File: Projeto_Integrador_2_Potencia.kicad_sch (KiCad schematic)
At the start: 18 parts, among them J10 Borne_CMD_Interface, J2 Vi 24V, J3 Vo 48V, J4 INA219_01x02_Socket_3.5mm, J5 INA219_01x06_Socket_2.55mm, J7 Display_01x04_Socket, J9 JST_01x02_Pin, Q1 IRF740

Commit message: Adição de footprint e símbolo do ESP32
Atualização das trilhas da PCB
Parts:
- removed ESP32_Socket_L, ESP32_Socket_R: ~, Connector_PinSocket_2.54mm:PinSocket_1x15_P2.54mm_Vertical, symbol Connector:Conn_01x15_Socket
- added U1: ESP32-DEVKIT-V1, footprints_and_symbols:MODULE_ESP32_DEVKIT_V1, symbol ESP32-DEVKIT-V1:ESP32-DEVKIT-V1
- J9: value JST_01x02_Pin -> PWM_Connector
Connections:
- net 12V: now also U1.30 (VIN)
- net 3V3: now also U1.1 (3V3)
- net GND: now also U1.2 (GND), U1.29 (GND)
- net I2C_Scl: now also U1.14 (D22)
- net I2C_Sda: now also U1.11 (D21)
- no-connect marks 0 -> 26
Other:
- note removed: "ESP32 DevKitV1 Socket"

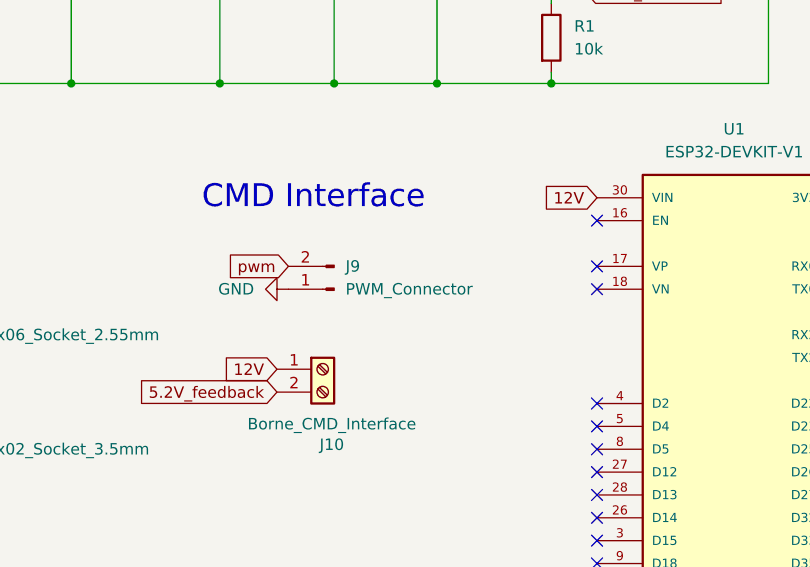
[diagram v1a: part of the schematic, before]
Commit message: Correções do layout da pcb e alinhamento do grupo
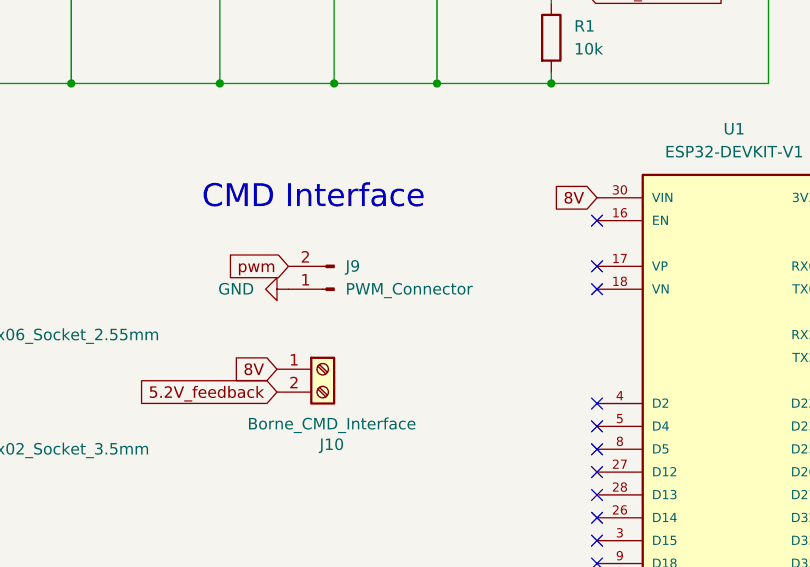
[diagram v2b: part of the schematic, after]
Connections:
- net 12V renamed 8V
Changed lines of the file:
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@@
 		)
 	)
-	(global_label "12V"
+	(global_label "8V"
 		(shape input)
 		(at 130.81 85.09 180)
@@
 		)
 		(property "Intersheetrefs" "${INTERSHEET_REFS}"
-			(at 124.3172 85.09 0)
+			(at 125.5267 85.09 0)
 			(effects
 				(font
@@
 		)
 	)
-	(global_label "12V"
+	(global_label "8V"
 		(shape input)
 		(at 95.25 104.14 180)
@@
 		)
 		(property "Intersheetrefs" "${INTERSHEET_REFS}"
-			(at 88.7572 104.14 0)
+			(at 89.9667 104.14 0)
 			(effects
 				(font

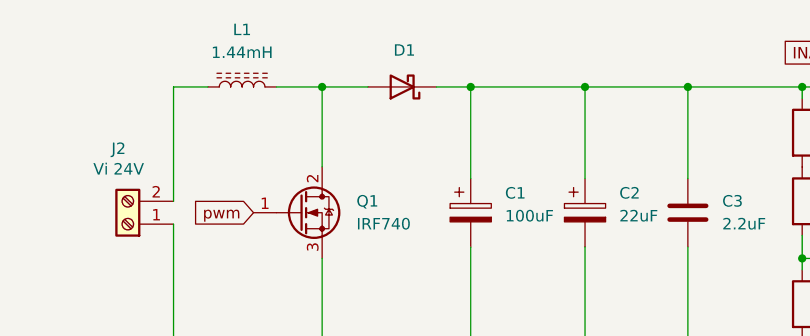
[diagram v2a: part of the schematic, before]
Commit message: Adição de recuo nas bordas do layout
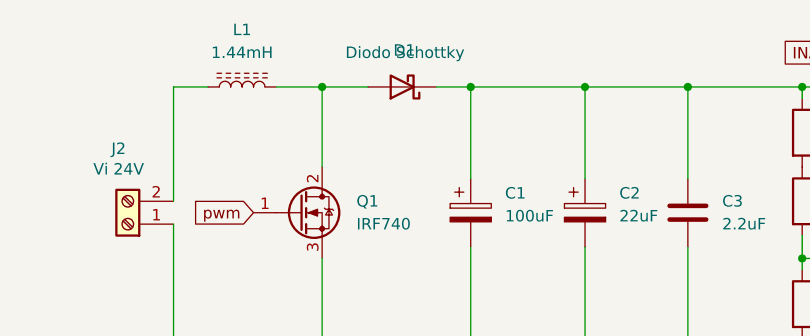
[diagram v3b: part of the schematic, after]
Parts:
- D1: value ~ -> Diodo Schottky
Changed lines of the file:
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@@
 			)
 		)
-		(property "Value" "~"
+		(property "Value" "Diodo Schottky"
 			(at 81.5975 39.37 0)
 			(effects

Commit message: Mudanças após primeira manufatura
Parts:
- added Q2: 47N60, Package_TO_SOT_THT:TO-247-3_Vertical, symbol Transistor_FET:C3M0280090D
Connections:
- net GND: now also Q2.3 (S)
- net pwm: now also Q2.1 (G)
- net at D1.2 (A), L1.2, Q1.2 (D): now also Q2.2 (D)
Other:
- moved on the sheet: J2, L1

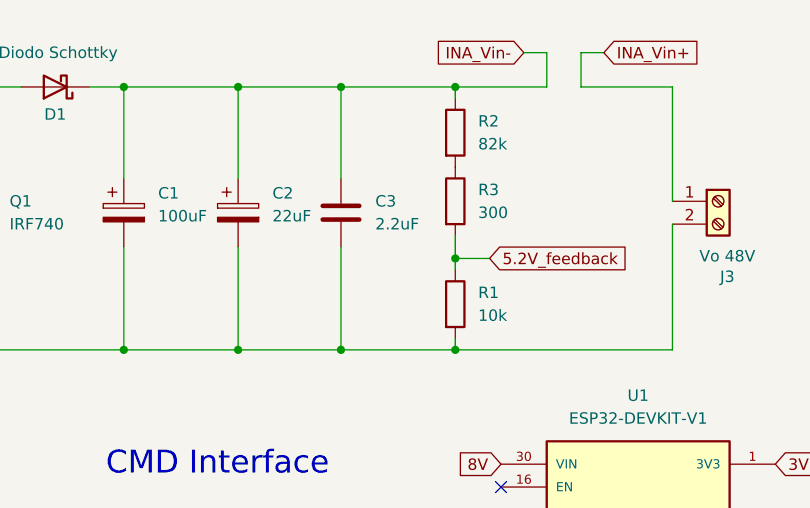
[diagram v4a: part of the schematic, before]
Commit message: Alargamento de trilhas e pads
Correção do valor do capacitor cerâmico
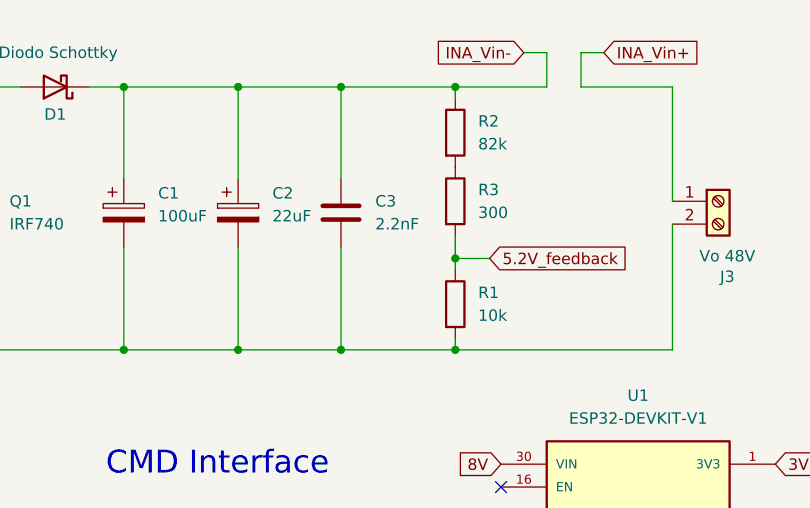
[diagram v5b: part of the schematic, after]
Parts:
- C3: value 2.2uF -> 2.2nF
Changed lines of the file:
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@@
 			)
 		)
-		(property "Value" "2.2uF"
+		(property "Value" "2.2nF"
 			(at 116.84 58.4199 0)
 			(effects
